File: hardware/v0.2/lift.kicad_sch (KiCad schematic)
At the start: 13 parts, among them J8 Molex Mini Fit Jr 39-30-1060, U5 DRV8874PWPR

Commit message: Finalize for production
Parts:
- J8: FT Position Offset (none) -> 0,3.81; LCSC (none) -> C114098
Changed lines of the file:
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@@
+			)
+		)
+		(property "LCSC" "C114098"
+			(at 220.98 118.11 0)
+			(effects
+				(font
+					(size 1.27 1.27)
+				)
+				(hide yes)
+			)
+		)
+		(property "FT Position Offset" "0,3.81"
+			(at 220.98 118.11 0)
+			(effects
+				(font
+					(size 1.27 1.27)
+				)
+				(hide yes)
 			)
 		)

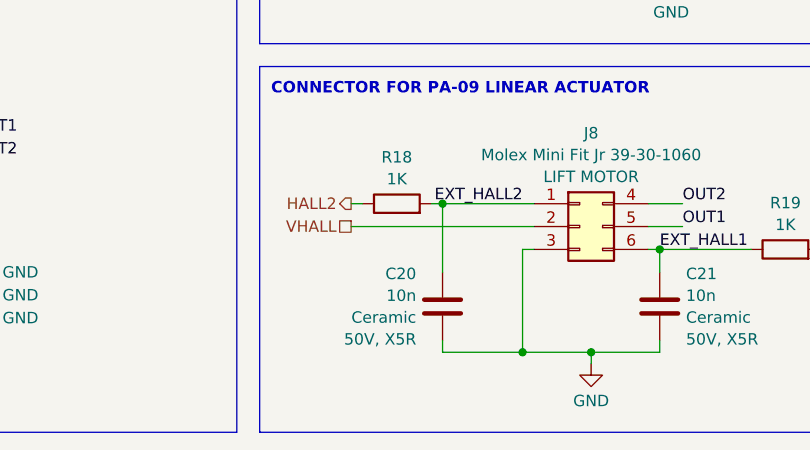
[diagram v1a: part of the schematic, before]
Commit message: Fix errata in v0.2, reversed lift motor pins 2 and 3.
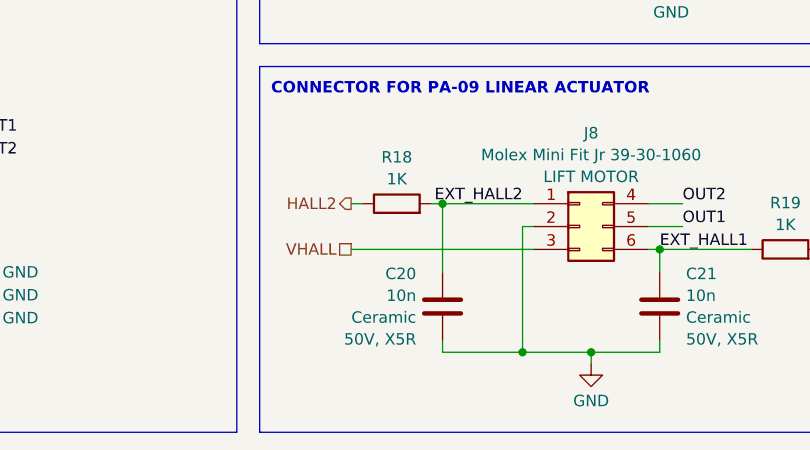
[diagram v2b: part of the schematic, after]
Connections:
- net GND: now also J8.2 (Pin_2); no longer J8.3 (Pin_3)
- net VHALL: now also J8.3 (Pin_3); no longer J8.2 (Pin_2)
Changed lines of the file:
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@@
 		(title "Bed Lift Controller")
 		(date "2025-10")
-		(rev "v0.2")
+		(rev "v0.2.1")
 		(company "Brown Studios LLC")
 	)
@@
 	(wire
 		(pts
-			(xy 214.63 120.65) (xy 215.9 120.65)
-		)
-		(stroke
-			(width 0)
-			(type default)
-		)
-	)
-	(wire
-		(pts
 			(xy 101.6 83.82) (xy 101.6 82.55)
 		)
@@
 	(wire
 		(pts
-			(xy 214.63 120.65) (xy 214.63 132.08)
-		)
-		(stroke
-			(width 0)
-			(type default)
-		)
-	)
-	(wire
-		(pts
 			(xy 205.74 130.81) (xy 205.74 132.08)
 		)
@@
 	(wire
 		(pts
-			(xy 195.58 118.11) (xy 215.9 118.11)
-		)
-		(stroke
-			(width 0)
-			(type default)
-		)
-	)
-	(wire
-		(pts
 			(xy 151.13 125.73) (xy 153.67 125.73)
 		)
@@
 	(wire
 		(pts
+			(xy 195.58 120.65) (xy 215.9 120.65)
+		)
+		(stroke
+			(width 0)
+			(type default)
+		)
+	)
+	(wire
+		(pts
 			(xy 205.74 115.57) (xy 205.74 123.19)
 		)
@@
 	(wire
 		(pts
+			(xy 214.63 118.11) (xy 215.9 118.11)
+		)
+		(stroke
+			(width 0)
+			(type default)
+		)
+	)
+	(wire
+		(pts
 			(xy 229.87 132.08) (xy 222.25 132.08)
 		)
@@
 		(pts
 			(xy 101.6 82.55) (xy 110.49 82.55)
+		)
+		(stroke
+			(width 0)
+			(type default)
+		)
+	)
+	(wire
+		(pts
+			(xy 214.63 118.11) (xy 214.63 132.08)
 		)
 		(stroke
@@
 	(hierarchical_label "VHALL"
 		(shape passive)
-		(at 195.58 118.11 180)
-		(effects
-			(font
+		(at 195.58 120.65 180)
+		(effects
+			(font
